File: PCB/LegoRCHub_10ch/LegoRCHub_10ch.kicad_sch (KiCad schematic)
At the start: 37 parts, among them J1 Conn_01x02, J10 Conn_01x03, J11 Conn_01x03_MountingPin, J12 Conn_01x02, J13 Conn_01x01, J2 Conn_01x02, J3 Conn_01x02, J4 Conn_01x02, J5 Conn_01x02, J6 Conn_01x02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

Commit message: Lego RC Hub 10ch: v4
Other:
- title: Lego RC Hub 10ch v3 -> Lego RC Hub 10ch v4
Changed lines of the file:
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@@
 	(paper "A4")
 	(title_block
-		(title "Lego RC Hub 10ch v3")
+		(title "Lego RC Hub 10ch v4")
 	)
 	(junction

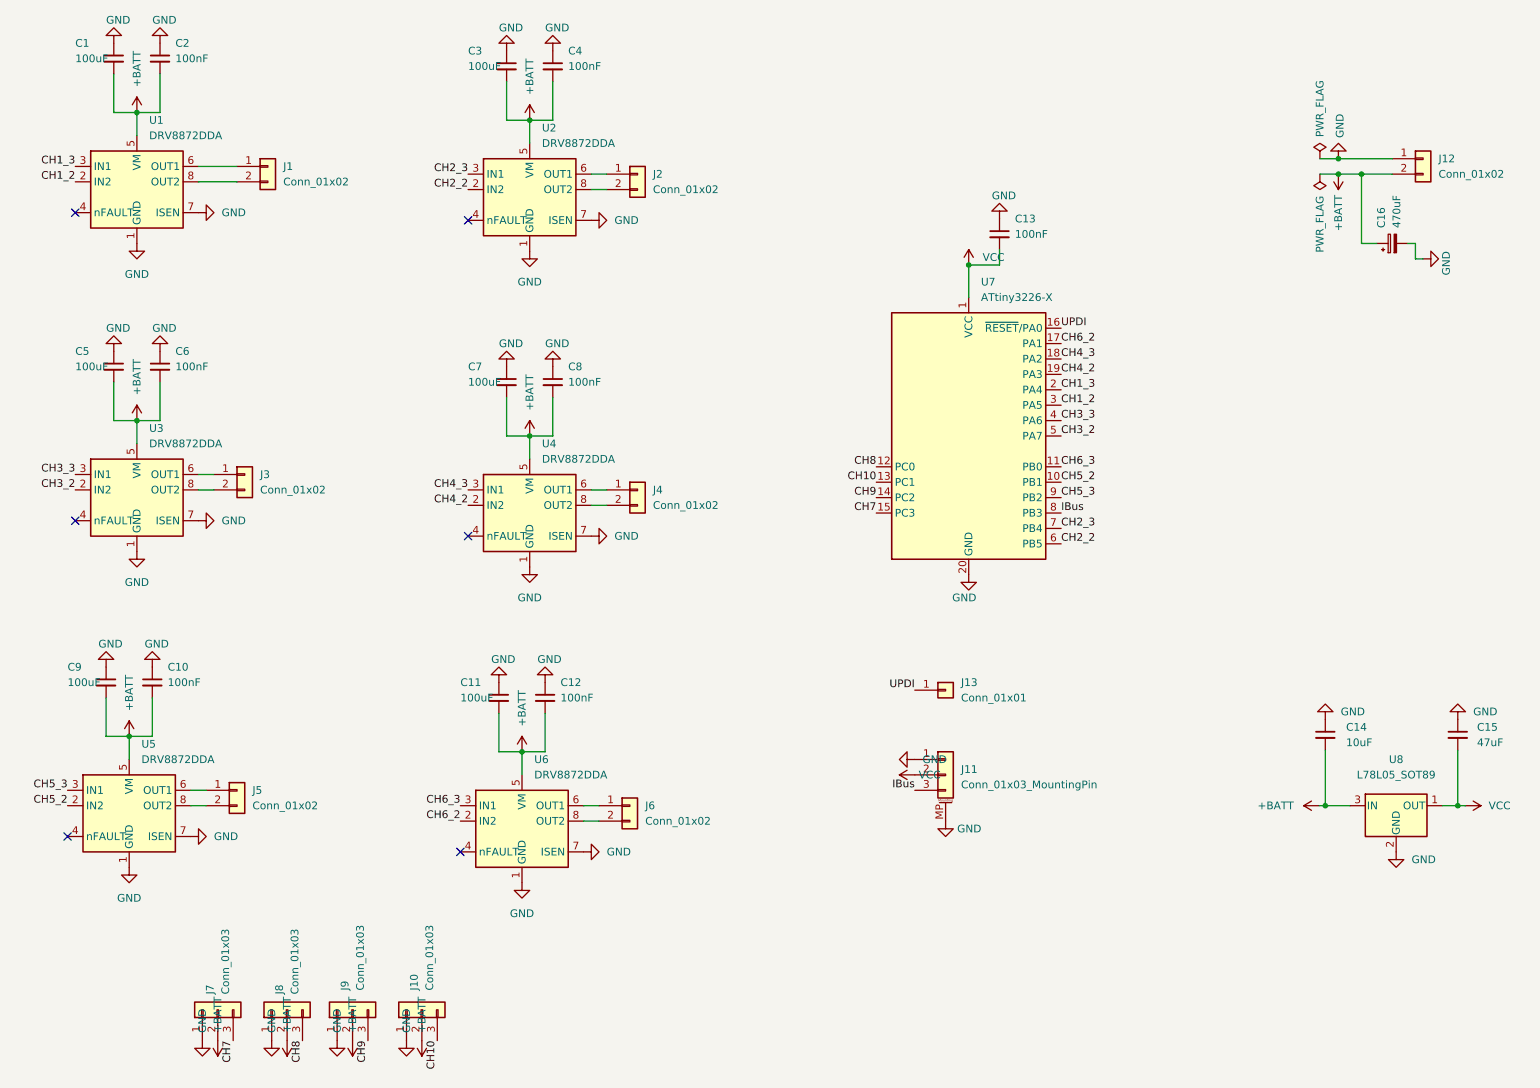
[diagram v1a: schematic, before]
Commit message: Lego RC Hub 10ch: minor tweaking for better rule compliance
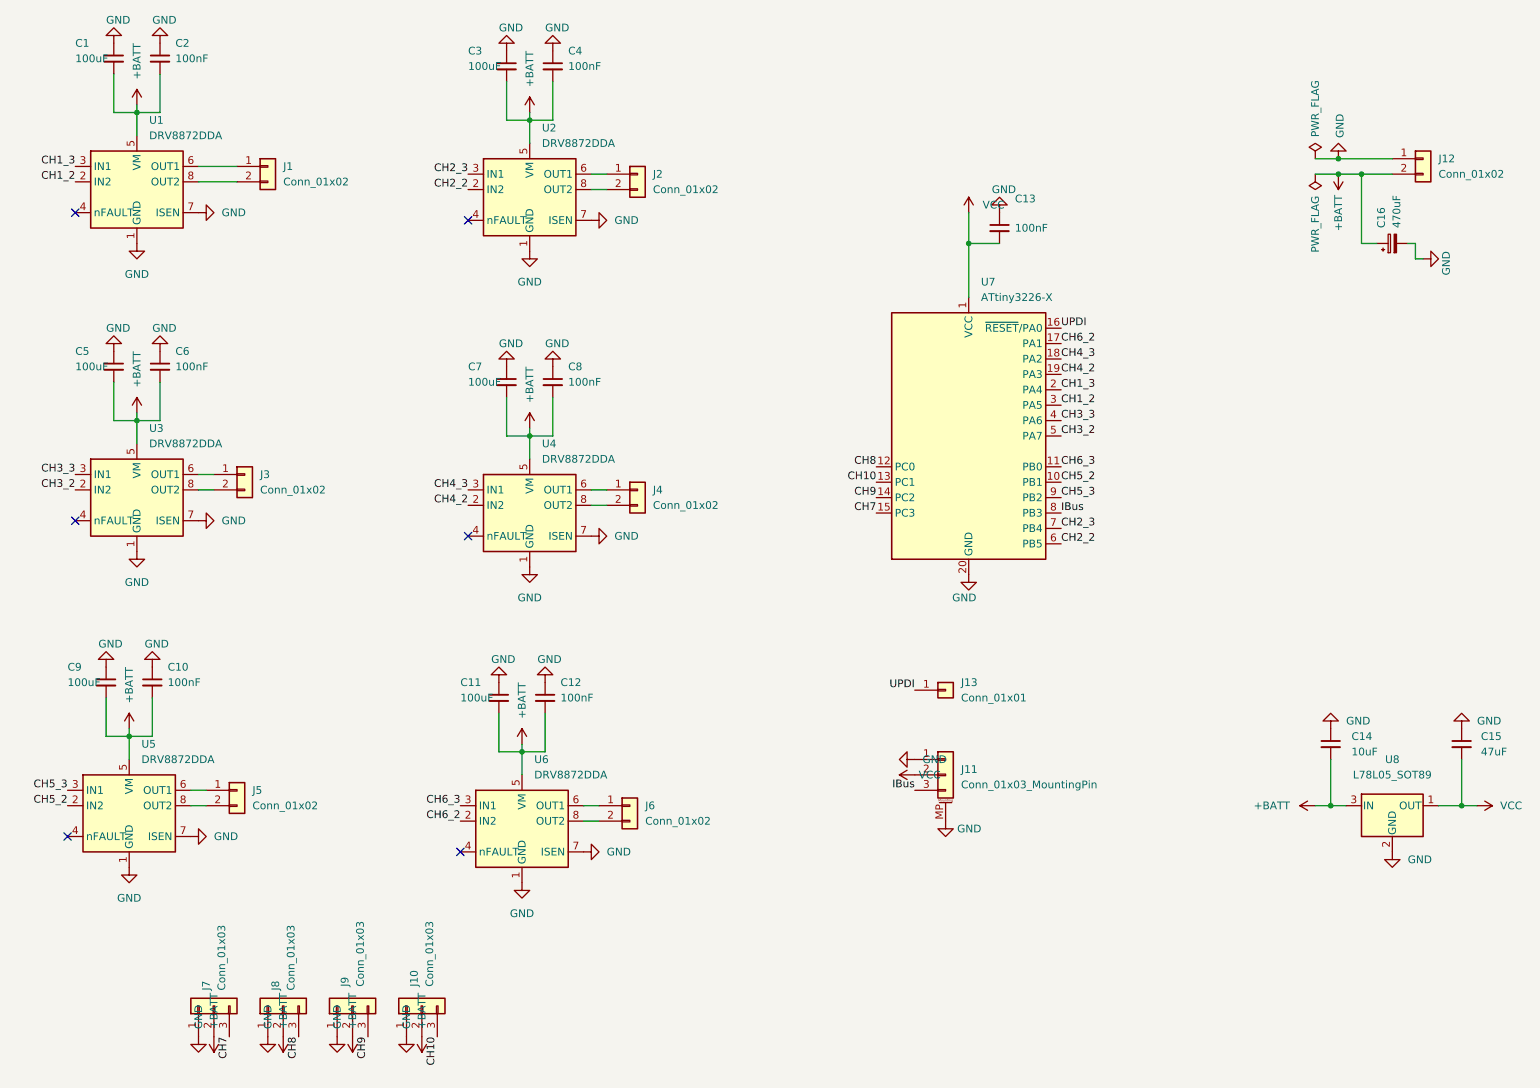
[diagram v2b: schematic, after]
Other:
- moved on the sheet: C13, C14, C15, J10, J7, J8, J9, U8

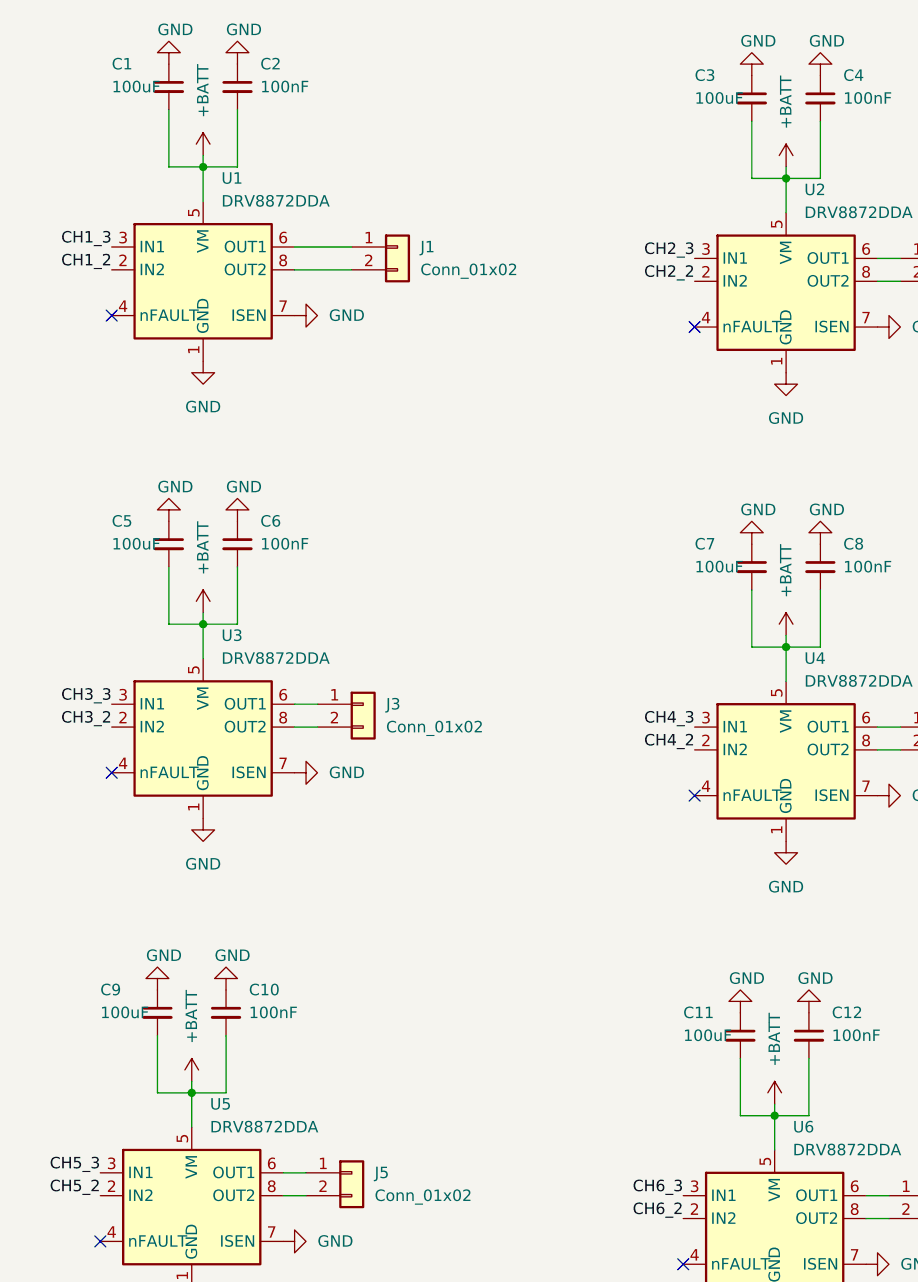
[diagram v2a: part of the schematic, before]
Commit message: Lego RC Hub 10ch: v5: added additional capacitors on channels + remade all vias
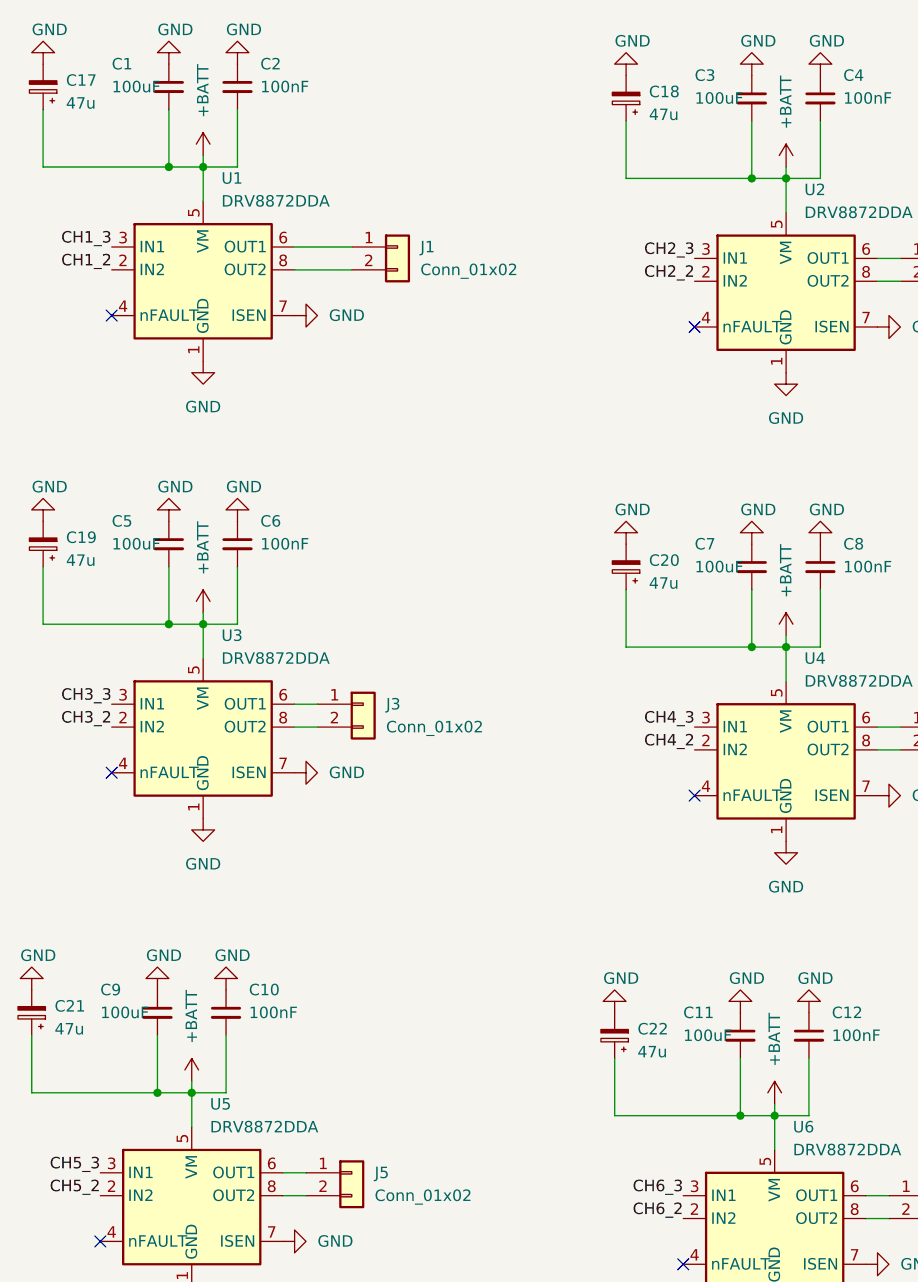
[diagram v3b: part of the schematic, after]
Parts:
- added C17, C18, C19, C20, C21, C22: 47u, Capacitor_SMD:CP_Elec_5x5.4, symbol Device:C_Polarized_Small
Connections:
- net +BATT: now also C17.1, C18.1, C19.1, C20.1, C21.1, C22.1
- net GND: now also C17.2, C18.2, C19.2, C20.2, C21.2, C22.2
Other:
- title: Lego RC Hub 10ch v4 -> Lego RC Hub 10ch v5

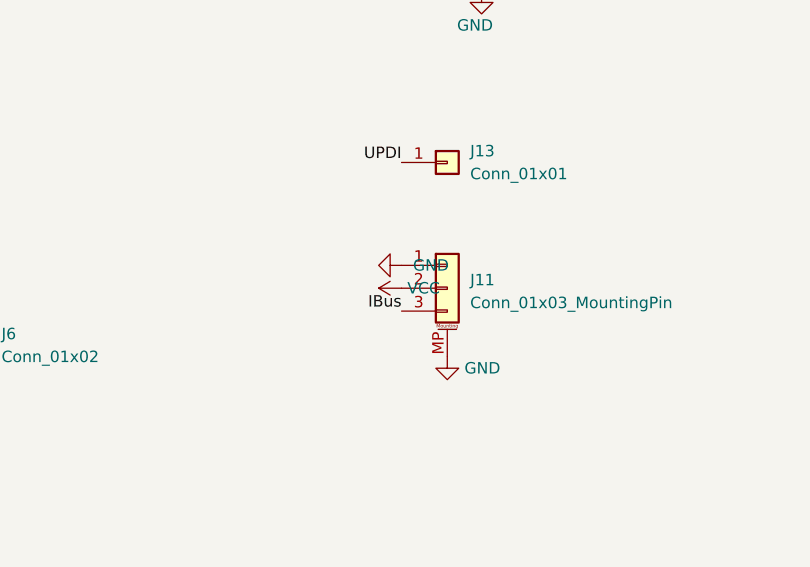
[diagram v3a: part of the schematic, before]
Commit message: PCB v6: inverted connector (as it should be)
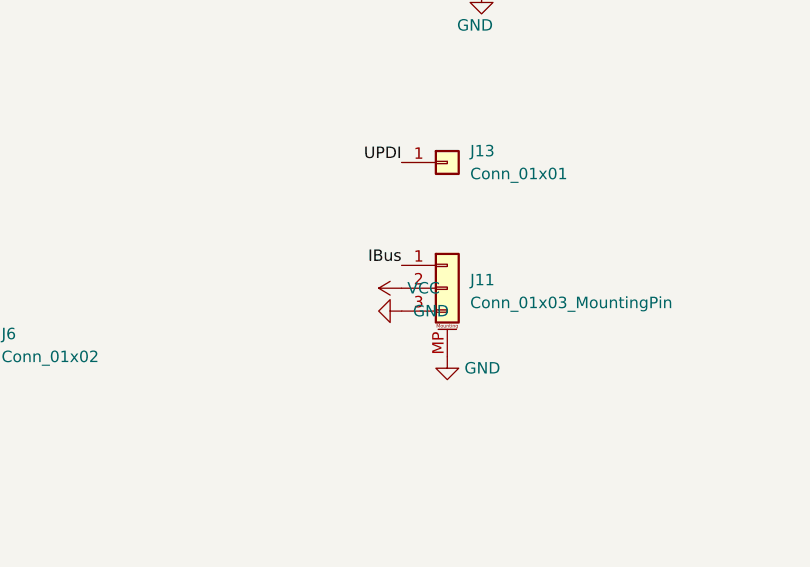
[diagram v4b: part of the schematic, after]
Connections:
- net GND: now also J11.3 (Pin_3); no longer J11.1 (Pin_1)
- net IBus: now also J11.1 (Pin_1); no longer J11.3 (Pin_3)
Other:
- title: Lego RC Hub 10ch v5 -> Lego RC Hub 10ch v6
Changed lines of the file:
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@@
 	(paper "A4")
 	(title_block
-		(title "Lego RC Hub 10ch v5")
+		(title "Lego RC Hub 10ch v6")
 	)
 	(junction
@@
 	)
 	(label "IBus"
-		(at 170.18 146.05 180)
+		(at 170.18 140.97 180)
 		(effects
 			(font
@@
 	(symbol
 		(lib_id "power:GND")
-		(at 170.18 140.97 270)
+		(at 170.18 146.05 270)
 		(unit 1)
 		(exclude_from_sim no)
@@
 		(fields_autoplaced yes)
 		(property "Reference" "#PWR043"
-			(at 163.83 140.97 0)
+			(at 163.83 146.05 0)
 			(effects
 				(font
@@
 		)
 		(property "Value" "GND"
-			(at 171.45 140.9699 90)
+			(at 171.45 146.0499 90)
 			(effects
 				(font
@@
 		)
 		(property "Footprint" ""
-			(at 170.18 140.97 0)
+			(at 170.18 146.05 0)
 			(effects
 				(font
@@
 		)
 		(property "Datasheet" ""
-			(at 170.18 140.97 0)
+			(at 170.18 146.05 0)
 			(effects
 				(font
@@
 		)
 		(property "Description" "Power symbol creates a global label with name \"GND\" , ground"
-			(at 170.18 140.97 0)
+			(at 170.18 146.05 0)
 			(effects
 				(font

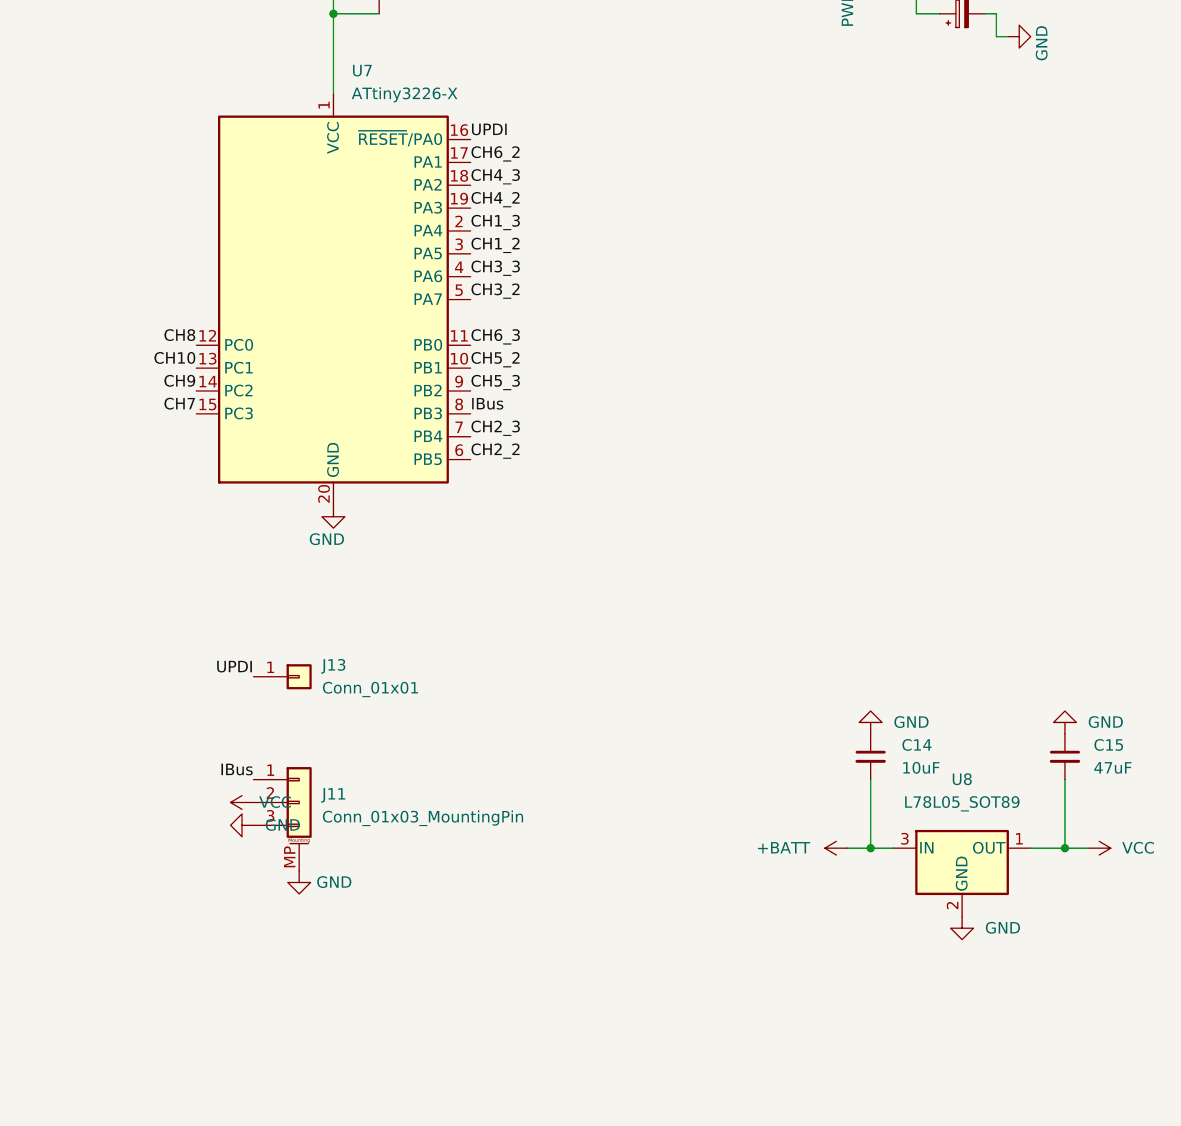
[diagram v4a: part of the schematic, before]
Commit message: PCB v7: added switch for microprocessor on/off
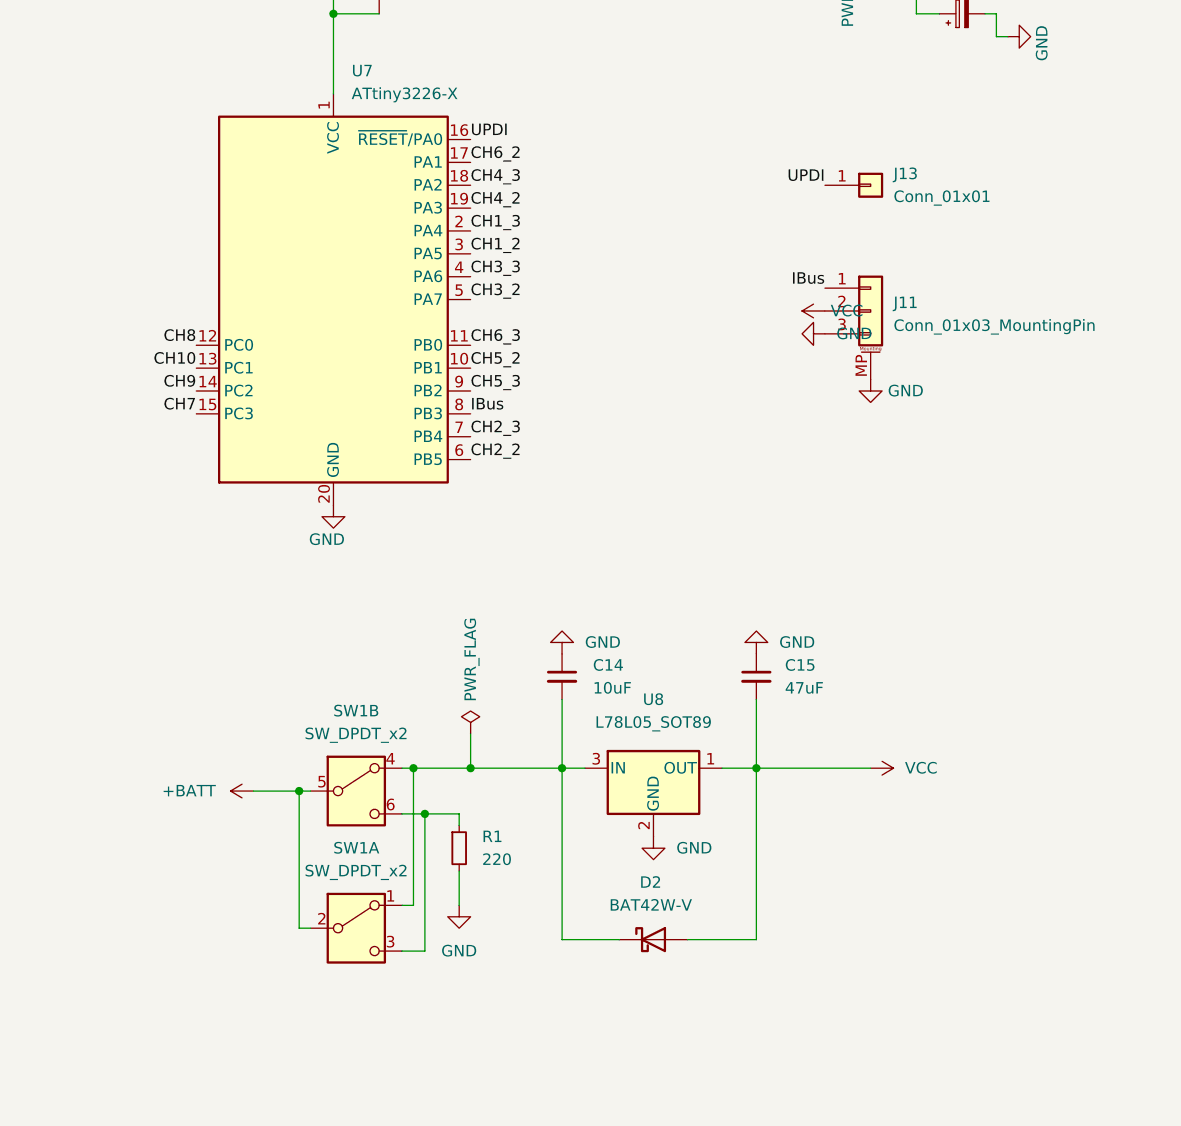
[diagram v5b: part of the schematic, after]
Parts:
- added D2: BAT42W-V, Diode_SMD:D_SOD-123, symbol Diode:BAT42W-V
- added R1: 220, Resistor_SMD:R_0805_2012Metric_Pad1.20x1.40mm_HandSolder, symbol Device:R_Small
- added SW1: SW_DPDT_x2, symbol Switch:SW_DPDT_x2
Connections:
- net +BATT: now also SW1.2 (B), SW1.5 (B); no longer C14.2, U8.3 (IN)
- net GND: now also R1.2
- net VCC: now also D2.2 (A)
- new net: C14.2, D2.1 (K), SW1.1 (A), SW1.4 (A), U8.3 (IN)
- new net: R1.1, SW1.3 (C), SW1.6 (C)
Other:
- title: Lego RC Hub 10ch v6 -> Lego RC Hub 10ch v7
- moved on the sheet: C14, C15, J11, J13, U8
